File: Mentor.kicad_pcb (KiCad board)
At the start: 2 copper layers, 50 x 100 mm, 41 parts, among them J1 CONN_01X02, J2 CONN_01X06, J3 CONN_01X09, J4 CONN_01X10, J5 CONN_01X02, J6 CONN_01X03, J7 CONN_01X09, Q1 PZT2222A, Q2 PZT2222A, Q3 IRFR3303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

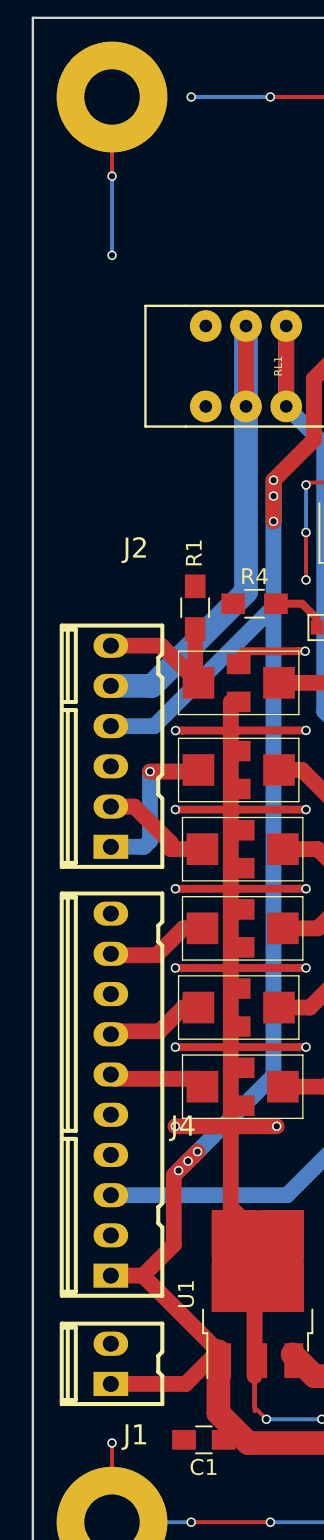
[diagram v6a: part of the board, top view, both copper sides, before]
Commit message: RTM2, via, prototype picture, gerber added
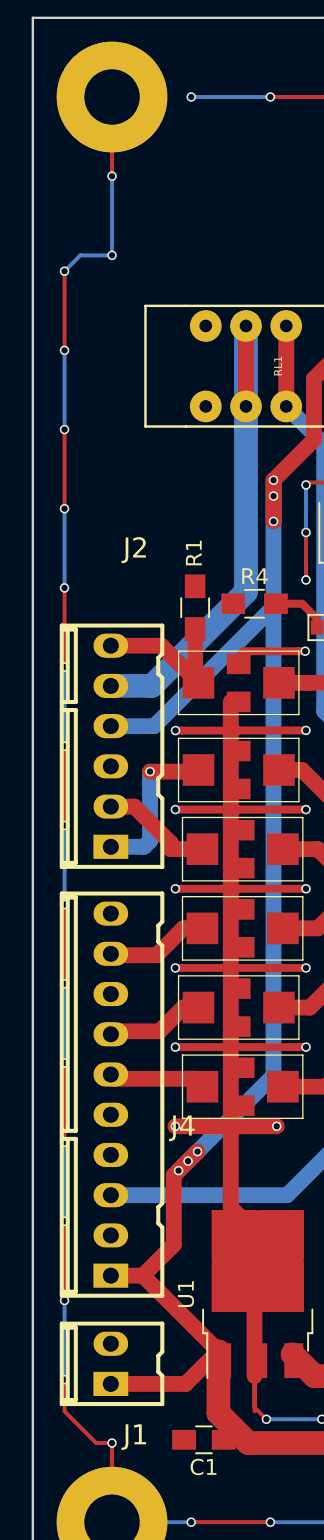
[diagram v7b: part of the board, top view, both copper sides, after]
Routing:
- net GND: track 308.6 -> 387.9 mm, vias 68 -> 83
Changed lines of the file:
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@@
     (links 112)
     (no_connects 0)
-    (area 159.924999 34.924999 210.075001 135.075001)
+    (area 148.5808 34.525 219.0716 135.575)
     (thickness 1.6)
     (drawings 12)
-    (tracks 396)
+    (tracks 430)
     (zones 0)
     (modules 41)
@@
   )
   (setup
-    (last_trace_width 0.5)
+    (last_trace_width 0.25)
     (user_trace_width 0.5)
     (user_trace_width 1)
@@
     (visible_elements 7FFFFFFF)
     (pcbplotparams
-      (layerselection 0x010fc_80000001)
+      (layerselection 0x010f0_80000001)
       (usegerberextensions true)
       (excludeedgelayer true)
@@
       (drillshape 0)
       (scaleselection 1)
-      (outputdirectory ../../../../Desktop/gerber_mentor/))
+      (outputdirectory Gerber/))
   )
   (net 0 "")
@@
     (effects (font (size 1 1) (thickness 0.25)) (justify mirror))
   )
-  (gr_text "TX/RX Status\nTXRX_Rly\n+12V\nGnd\nREFL\nFWD" (at 167.2 81) (layer B.SilkS)
+  (gr_text "TX/RX Status\nTXRX_Rly\n+12V\nGnd\nREFL\nFWD" (at 167 81) (layer B.SilkS)
     (effects (font (size 1.5 1.5) (thickness 0.3)) (justify right mirror))
   )
@@
   (segment (start 191 125) (end 189.5 125) (width 1.5) (layer F.Cu) (net 3))
   (segment (start 201 115) (end 191 125) (width 1.5) (layer F.Cu) (net 3))
+  (segment (start 165 125) (end 164 125) (width 0.25) (layer F.Cu) (net 4))
+  (via (at 165 125) (size 0.6) (drill 0.4) (layers F.Cu B.Cu) (net 4))
+  (segment (start 165 130) (end 165 125) (width 0.25) (layer F.Cu) (net 4) (status 10))
+  (via (at 165 45) (size 0.6) (drill 0.4) (layers F.Cu B.Cu) (net 4))
+  (segment (start 165 45) (end 165 50) (width 0.25) (layer B.Cu) (net 4))
+  (via (at 165 50) (size 0.6) (drill 0.4) (layers F.Cu B.Cu) (net 4))
+  (segment (start 165 45) (end 165 40) (width 0.25) (layer F.Cu) (net 4) (status 10))
+  (segment (start 163 50) (end 165 50) (width 0.25) (layer B.Cu) (net 4))
+  (segment (start 162 51) (end 163 50) (width 0.25) (layer B.Cu) (net 4))
+  (via (at 162 51) (size 0.6) (drill 0.4) (layers F.Cu B.Cu) (net 4))
+  (segment (start 162 56) (end 162 51) (width 0.25) (layer F.Cu) (net 4))
+  (via (at 162 56) (size 0.6) (drill 0.4) (layers F.Cu B.Cu) (net 4))
+  (segment (start 162 61) (end 162 56) (width 0.25) (layer B.Cu) (net 4))
+  (via (at 162 61) (size 0.6) (drill 0.4) (layers F.Cu B.Cu) (net 4))
+  (segment (start 162 66) (end 162 61) (width 0.25) (layer F.Cu) (net 4))
+  (via (at 162 66) (size 0.6) (drill 0.4) (layers F.Cu B.Cu) (net 4))
+  (segment (start 162 71) (end 162 66) (width 0.25) (layer B.Cu) (net 4))
+  (via (at 162 71) (size 0.6) (drill 0.4) (layers F.Cu B.Cu) (net 4))
+  (segment (start 162 76) (end 162 71) (width 0.25) (layer F.Cu) (net 4))
+  (via (at 162 76) (size 0.6) (drill 0.4) (layers F.Cu B.Cu) (net 4))
+  (segment (start 162 81) (end 162 76) (width 0.25) (layer B.Cu) (net 4))
+  (via (at 162 81) (size 0.6) (drill 0.4) (layers F.Cu B.Cu) (net 4))
+  (segment (start 162 86) (end 162 81) (width 0.25) (layer F.Cu) (net 4))
+  (via (at 162 86) (size 0.6) (drill 0.4) (layers F.Cu B.Cu) (net 4))
+  (segment (start 162 91) (end 162 86) (width 0.25) (layer B.Cu) (net 4))
+  (via (at 162 91) (size 0.6) (drill 0.4) (layers F.Cu B.Cu) (net 4))
+  (segment (start 162 96) (end 162 91) (width 0.25) (layer F.Cu) (net 4))
+  (via (at 162 96) (size 0.6) (drill 0.4) (layers F.Cu B.Cu) (net 4))
+  (segment (start 162 101) (end 162 96) (width 0.25) (layer B.Cu) (net 4))
+  (via (at 162 101) (size 0.6) (drill 0.4) (layers F.Cu B.Cu) (net 4))
+  (segment (start 162 106) (end 162 101) (width 0.25) (layer F.Cu) (net 4))
+  (via (at 162 106) (size 0.6) (drill 0.4) (layers F.Cu B.Cu) (net 4))
+  (segment (start 162 111) (end 162 106) (width 0.25) (layer B.Cu) (net 4))
+  (via (at 162 111) (size 0.6) (drill 0.4) (layers F.Cu B.Cu) (net 4))
+  (segment (start 162 116) (end 162 111) (width 0.25) (layer F.Cu) (net 4))
+  (via (at 162 116) (size 0.6) (drill 0.4) (layers F.Cu B.Cu) (net 4))
+  (segment (start 162 121) (end 162 116) (width 0.25) (layer B.Cu) (net 4))
+  (via (at 162 121) (size 0.6) (drill 0.4) (layers F.Cu B.Cu) (net 4))
+  (segment (start 162 123) (end 162 121) (width 0.25) (layer F.Cu) (net 4))
+  (segment (start 164 125) (end 162 123) (width 0.25) (layer F.Cu) (net 4))
   (segment (start 192.54 106.225) (end 192.54 102.04) (width 0.25) (layer B.Cu) (net 4) (status 10))
   (via (at 192.5 100.5) (size 0.6) (drill 0.4) (layers F.Cu B.Cu) (net 4))
@@
   (segment (start 205 45) (end 205 50) (width 0.25) (layer B.Cu) (net 4))
   (via (at 205 45) (size 0.6) (drill 0.4) (layers F.Cu B.Cu) (net 4))
-  (segment (start 165 40) (end 165 45) (width 0.25) (layer F.Cu) (net 4) (status 10))
-  (via (at 165 50) (size 0.6) (drill 0.4) (layers F.Cu B.Cu) (net 4))
-  (segment (start 165 45) (end 165 50) (width 0.25) (layer B.Cu) (net 4))
-  (via (at 165 45) (size 0.6) (drill 0.4) (layers F.Cu B.Cu) (net 4))
   (segment (start 205 40) (end 200 40) (width 0.25) (layer B.Cu) (net 4) (status 10))
   (via (at 170 40) (size 0.6) (drill 0.4) (layers F.Cu B.Cu) (net 4))
@@
   (via (at 200 130) (size 0.6) (drill 0.4) (layers F.Cu B.Cu) (net 4))
   (via (at 165 130) (size 0.6) (drill 0.4) (layers F.Cu B.Cu) (net 4) (status 30))
-  (segment (start 165 130) (end 165 125) (width 0.25) (layer F.Cu) (net 4) (status 10))
-  (via (at 165 125) (size 0.6) (drill 0.4) (layers F.Cu B.Cu) (net 4))
   (segment (start 205.5762 109.27) (end 203.27 109.27) (width 0.25) (layer B.Cu) (net 4) (status 10))
   (segment (start 203.27 109.27) (end 203 109) (width 0.25) (layer B.Cu) (net 4))

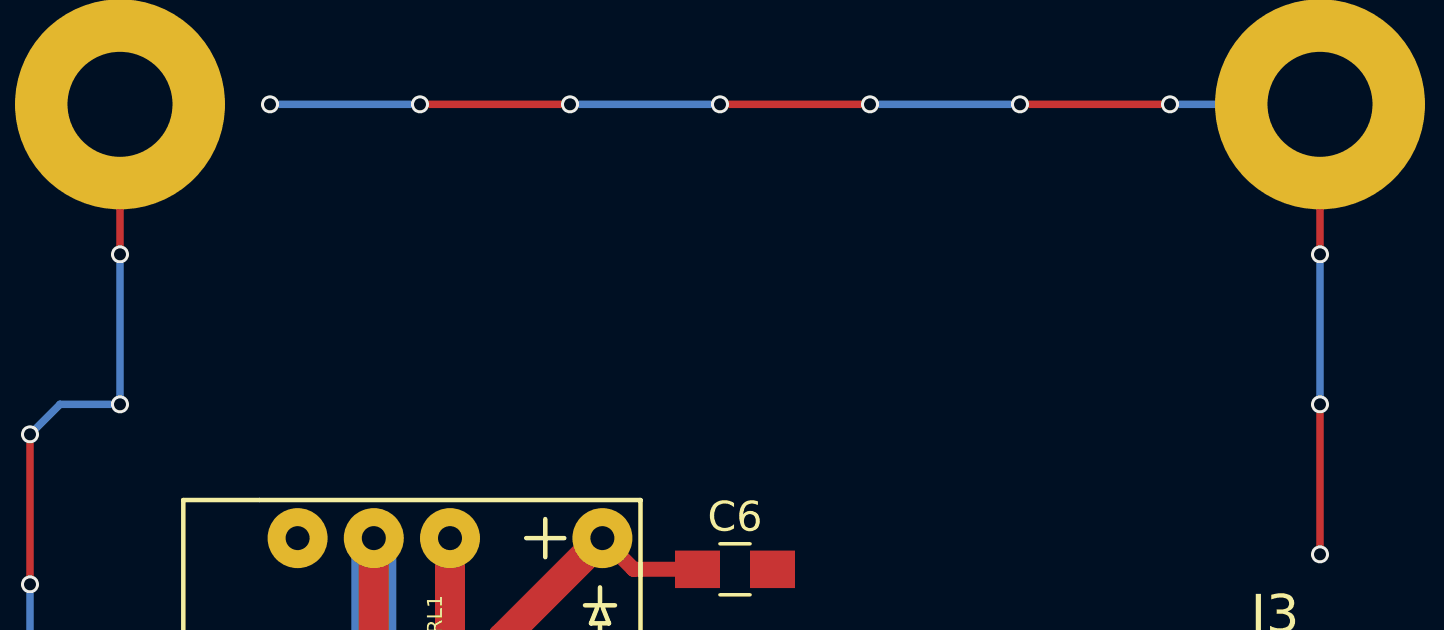
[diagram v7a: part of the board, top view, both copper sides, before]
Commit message: Silkmask comment added
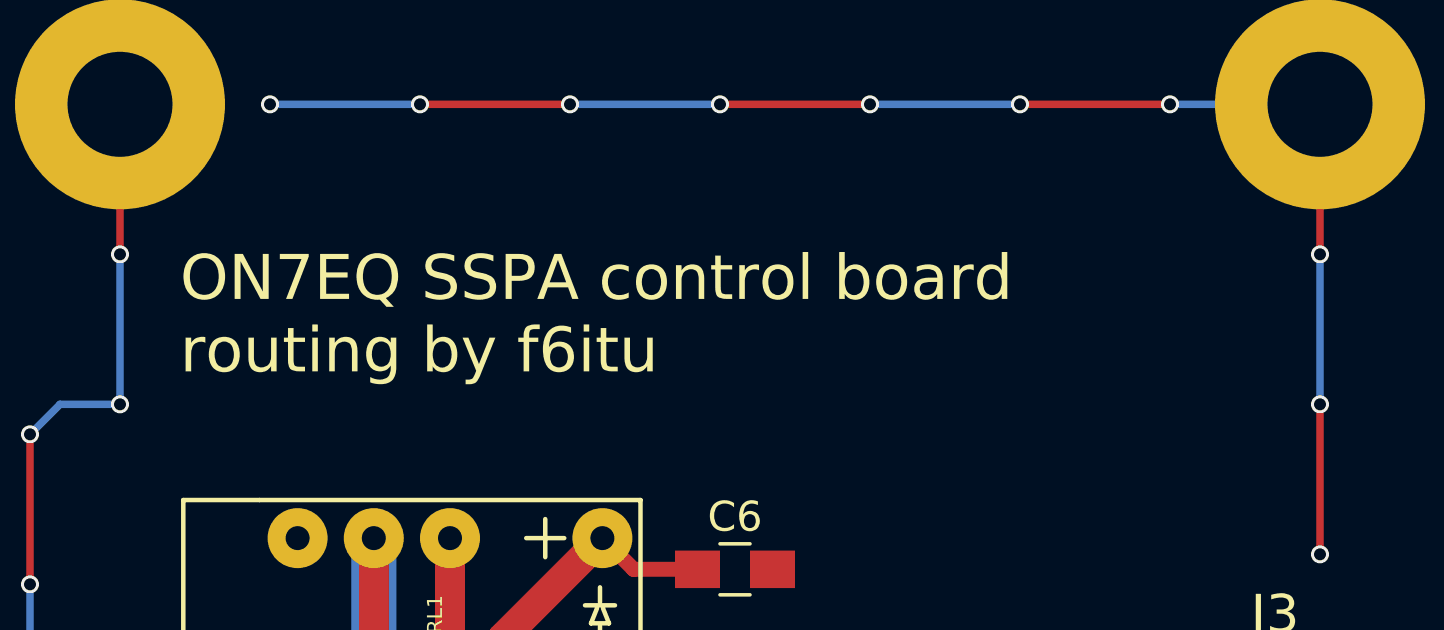
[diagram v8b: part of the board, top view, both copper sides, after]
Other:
- board text added: "ON7EQ SSPA control board routing by f6itu"
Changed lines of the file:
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@@
     (area 148.5808 34.525 219.0716 135.575)
     (thickness 1.6)
-    (drawings 12)
+    (drawings 13)
     (tracks 430)
     (zones 0)
@@
     )
   )
+  (gr_text "ON7EQ SSPA control board\nrouting by f6itu" (at 167 47) (layer F.SilkS)
+    (effects (font (size 1.5 1.5) (thickness 0.3)) (justify left))
+  )
   (gr_line (start 160 135) (end 160 35) (angle 90) (layer Edge.Cuts) (width 0.15))
